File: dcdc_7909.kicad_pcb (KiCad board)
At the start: 2 copper layers, 36.8 x 26 mm, 28 parts, among them J1 V_IN, J2 G_IN, J3 +10V, J4 G_OUT, J5 -10V, U1 TMR6, U2 LT3045xMSE, U3 LT3094xMSE

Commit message: V2 PCB almost finished.
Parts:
- removed the C13 at (96.4, 76.8)
- removed the C14 at (106.4, 57.6)
- added C10: 22u, Capacitor_SMD:C_0805_2012Metric_Pad1.18x1.45mm_HandSolder, F.Cu at (91.9, 59.5)
- added C19: C_Polarized_Small, Capacitor_Tantalum_SMD:CP_EIA-3528-21_Kemet-B_Pad1.50x2.35mm_HandSolder, F.Cu at (89.0, 62.1)
- added C21: C_Polarized_Small, Capacitor_Tantalum_SMD:CP_EIA-3528-21_Kemet-B_Pad1.50x2.35mm_HandSolder, F.Cu at (94.2, 78.0)
- added C4: 2200p, Capacitor_SMD:C_0603_1608Metric, F.Cu at (107.1, 68.8)
- added C5: 22u, Capacitor_SMD:C_0805_2012Metric_Pad1.18x1.45mm_HandSolder, F.Cu at (107.5, 78.7)
- added C6: 10n, Capacitor_SMD:C_0603_1608Metric, F.Cu at (107.1, 77.0)
- added C7: 10u X7R, Capacitor_SMD:C_0603_1608Metric, F.Cu at (101.7, 65.5)
- added C8: 10u X7R, Capacitor_SMD:C_0603_1608Metric, F.Cu at (103.3, 65.5)
- added C9: 470p, Capacitor_SMD:C_0603_1608Metric, F.Cu at (105.5, 65.0)
- added D1: D_Schottky, Diode_SMD:D_PowerDI-123, F.Cu at (103.5, 72.0)
- added D2: D_Schottky, Diode_SMD:D_PowerDI-123, F.Cu at (103.5, 62.2)
- added J3: RFShield_OnePiece, RF_Shielding:Laird_Technologies_BMI-S-102_16.50x16.50mm, F.Cu at (102.0, 67.3)
- added L1: 10u, Inductor_SMD:L_Vishay_IHLP-1616, F.Cu at (97.8, 71.6)
- added L2: 10u, Inductor_SMD:L_Vishay_IHLP-1616, F.Cu at (97.8, 66.9)
- added L3: 10u, Inductor_SMD:L_Vishay_IHLP-1616, F.Cu at (97.8, 62.3)
- added R1: 20k, Resistor_SMD:R_0603_1608Metric, F.Cu at (100.5, 77.1)
- added R2: 10k, Resistor_SMD:R_0603_1608Metric, F.Cu at (107.6, 70.4)
- added R3: 1.58k, Resistor_SMD:R_0603_1608Metric, F.Cu at (108.6, 65.1)
- added R4: 10k, Resistor_SMD:R_0603_1608Metric, F.Cu at (107.1, 65.1)
- added TP1: +10.5V, TestPoint:TestPoint_Pad_D2.0mm, B.Cu at (107.1, 77.9)
- added TP2: -10.5V, TestPoint:TestPoint_Pad_D2.0mm, B.Cu at (95.6, 58.5)
- C1: value 100u 25v -> 22u; footprint Capacitor_Tantalum_SMD:CP_EIA-7343-31_Kemet-D_Pad2.25x2.55mm_HandSolder -> Capacitor_SMD:C_0805_2012Metric_Pad1.18x1.45mm_HandSolder
- C11: value 100u 16V -> 10n; footprint Capacitor_Tantalum_SMD:CP_EIA-7343-31_Kemet-D_Pad2.25x2.55mm_HandSolder -> Capacitor_SMD:C_0603_1608Metric
- C12: renamed from C4; footprint Capacitor_SMD:C_1206_3216Metric_Pad1.42x1.75mm_HandSolder -> Capacitor_SMD:C_0805_2012Metric_Pad1.18x1.45mm_HandSolder
- C13: renamed from C5; footprint Capacitor_SMD:C_1206_3216Metric_Pad1.42x1.75mm_HandSolder -> Capacitor_SMD:C_0805_2012Metric_Pad1.18x1.45mm_HandSolder
- C14: renamed from C6; footprint Capacitor_SMD:C_1206_3216Metric_Pad1.42x1.75mm_HandSolder -> Capacitor_SMD:C_0805_2012Metric_Pad1.18x1.45mm_HandSolder
- C15: renamed from C7; footprint Capacitor_SMD:C_1206_3216Metric_Pad1.42x1.75mm_HandSolder -> Capacitor_SMD:C_0805_2012Metric_Pad1.18x1.45mm_HandSolder
- C16: renamed from C8; footprint Capacitor_SMD:C_1206_3216Metric_Pad1.42x1.75mm_HandSolder -> Capacitor_SMD:C_0805_2012Metric_Pad1.18x1.45mm_HandSolder
- C17: renamed from C9; footprint Capacitor_SMD:C_0603_1608Metric_Pad1.05x0.95mm_HandSolder -> Capacitor_SMD:C_0603_1608Metric
- C18: renamed from C10; footprint Capacitor_SMD:C_1206_3216Metric_Pad1.42x1.75mm_HandSolder -> Capacitor_SMD:C_0805_2012Metric_Pad1.18x1.45mm_HandSolder
- C2: value 100u 16V -> 10u X7R; footprint Capacitor_Tantalum_SMD:CP_EIA-7343-31_Kemet-D_Pad2.25x2.55mm_HandSolder -> Capacitor_SMD:C_0603_1608Metric
- C20: renamed from C12; footprint Capacitor_SMD:C_0603_1608Metric_Pad1.05x0.95mm_HandSolder -> Capacitor_SMD:C_0603_1608Metric
- C3: value 100u 16V -> 100n X7R; footprint Capacitor_Tantalum_SMD:CP_EIA-7343-31_Kemet-D_Pad2.25x2.55mm_HandSolder -> Capacitor_SMD:C_0603_1608Metric
- D3: renamed from D1; footprint LED_SMD:LED_0603_1608Metric_Pad1.05x0.95mm_HandSolder -> LED_SMD:LED_0805_2012Metric_Pad1.15x1.40mm_HandSolder
- D4: renamed from D2; footprint LED_SMD:LED_0603_1608Metric_Pad1.05x0.95mm_HandSolder -> LED_SMD:LED_0805_2012Metric_Pad1.15x1.40mm_HandSolder
- R5: renamed from R1; value 100k -> 100k 1%; footprint Resistor_SMD:R_0603_1608Metric_Pad1.05x0.95mm_HandSolder -> Resistor_SMD:R_0603_1608Metric
- R6: renamed from R2; value 100k -> 100k 1%; footprint Resistor_SMD:R_0603_1608Metric_Pad1.05x0.95mm_HandSolder -> Resistor_SMD:R_0603_1608Metric
- R7: renamed from R3; value 820 -> 1k; footprint Resistor_SMD:R_0805_2012Metric_Pad1.15x1.40mm_HandSolder -> Resistor_SMD:R_0603_1608Metric; moved to F.Cu
- R8: renamed from R4; value 820 -> 1k; footprint Resistor_SMD:R_0805_2012Metric_Pad1.15x1.40mm_HandSolder -> Resistor_SMD:R_0603_1608Metric; moved to F.Cu
- U1: value TMR6 -> LT3471; footprint marcin_library:Traco_TMR6 -> Package_DFN_QFN:DFN-10-1EP_3x3mm_P0.5mm_EP1.65x2.38mm
- moved C3 26.1 mm to (106.8, 67.3), turned to 0 degrees
- moved C2 24.2 mm to (102.2, 78.6), turned to 0 degrees
- moved C12 23.9 mm to (81.7, 78.5), turned to 180 degrees
- moved C20 21.8 mm to (80.8, 56.0), turned to 180 degrees
- moved C14 21.8 mm to (87.0, 55.4), turned to 0 degrees
- moved C16 21.5 mm to (80.3, 68.3), turned to 90 degrees
- moved R5 19.4 mm to (87.0, 57.1), turned to 0 degrees
- moved U2 14.6 mm to (83.8, 74.4), turned to 90 degrees
- moved C18 14.4 mm to (81.3, 58.7), turned to -90 degrees
- moved C11 13.3 mm to (92.3, 65.3), turned to -90 degrees
- moved C17 10.4 mm to (82.0, 68.0)
- moved C15 10.2 mm to (85.7, 68.7), turned to 0 degrees
- moved D3 10.1 mm to (93.3, 70.9)
- moved U1 9.97 mm to (103.1, 68.8)
- moved U3 9.50 mm to (85.0, 61.1), turned to 90 degrees
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- renumbered J3 to J4, J4 to J5, J5 to J6
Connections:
- net -12V renamed /-10V
- C11 pad 1: +12V -> /-10.5V
- C12 pad 1: Net-(C2-Pad1) -> /+10.5V
- C13 pad 1: Net-(C3-Pad2) -> /-10.5V
- C16 pad 1: +12V -> /+10V
- C17 pad 1: +12V -> /+10V
- C3 pad 1: GND -> Net-(C3-Pad1)
- C3 pad 2: Net-(C3-Pad2) -> GND
- J4 pad 1: +12V -> /+10V
- R7 pad 1: +12V -> /+10V
- U1 pad 1: GND -> Net-(C4-Pad2)
- U1 pad 2: VCC -> Net-(C3-Pad1)
- U1 pad 3: VCC -> Net-(C3-Pad1)
- U1 pad 5: Net-(U1-Pad5) -> GND
- U1 pad 6: Net-(C2-Pad1) -> Net-(C7-Pad1)
- U1 pad 7: GND -> Net-(C2-Pad1)
- U1 pad 8: Net-(C3-Pad2) -> VCC
- U2 pad 1: Net-(C2-Pad1) -> /+10.5V
- U2 pad 10: +12V -> /+10V
- U2 pad 11: +12V -> /+10V
- U2 pad 12: +12V -> /+10V
- U2 pad 2: Net-(C2-Pad1) -> /+10.5V
- U2 pad 3: Net-(C2-Pad1) -> /+10.5V
- U2 pad 4: Net-(C2-Pad1) -> /+10.5V
- U2 pad 5: Net-(U2-Pad5) -> unconnected-(U2-Pad5)
- U2 pad 7: Net-(C2-Pad1) -> /+10.5V
- U3 pad 1: Net-(C3-Pad2) -> /-10.5V
- U3 pad 13: Net-(C3-Pad2) -> /-10.5V
- U3 pad 2: Net-(C3-Pad2) -> /-10.5V
- U3 pad 3: Net-(C3-Pad2) -> /-10.5V
- U3 pad 4: Net-(U3-Pad4) -> unconnected-(U3-Pad4)
- U3 pad 5: Net-(C3-Pad2) -> /-10.5V
- U3 pad 7: Net-(U3-Pad7) -> unconnected-(U3-Pad7)
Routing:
- net /+10.5V: track 0.00 -> 47.4 mm, vias 0 -> 3
- net /-10.5V: track 0.00 -> 34.0 mm, vias 0 -> 10
- net VCC: track 16.9 -> 44.4 mm, vias 0 -> 3
- net /-10V: track 13.6 -> 33.9 mm, vias 0 -> 1
- net +12V: track 14.3 -> 0.00 mm, vias 1 -> 0
- net /+10V: track 0.00 -> 12.8 mm, vias 0 -> 1
- net Net-(C3-Pad2): track 12.1 -> 0.00 mm, vias 8 -> 0
- net Net-(C2-Pad1): track 26.3 -> 15.3 mm
- net Net-(C4-Pad2): track 0.00 -> 9.00 mm
- net Net-(C9-Pad2): track 0.00 -> 7.00 mm
- net Net-(D1-Pad2): track 0.00 -> 5.19 mm
- net Net-(C7-Pad2): track 0.00 -> 4.71 mm
- net Net-(C7-Pad1): track 0.00 -> 3.82 mm
- net Net-(C3-Pad1): track 0.00 -> 2.90 mm
- net Net-(C14-Pad1): track 5.02 -> 3.57 mm
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- added copper zone on F.Cu, net /+10.5V
- added copper zone on F.Cu, net /+10V
- added copper zone on B.Cu, net /-10.5V
- added copper zone on F.Cu, net /-10.5V
- removed copper zone on F.Cu, net +12V
- removed copper zone on F.Cu, net Net-(C2-Pad1)
- removed copper zone on B.Cu, net Net-(C3-Pad2)
- removed copper zone on F.Cu, net Net-(C3-Pad2)
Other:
- board size 36.8 x 26 mm -> 37 x 27 mm
- net class Default removed
- board text added: "+"
- board text added: "+10V"
- board text added: "-10V"
- board text added: "Alpine 7909 DC/DC v2.0 (c) M. Dymczyk 07.2023"
- board text removed: "Alpine 7909 DC/DC v1.1 (c) M. Dymczyk 04.2020"
- board text removed: "Traco TMR6-1222"

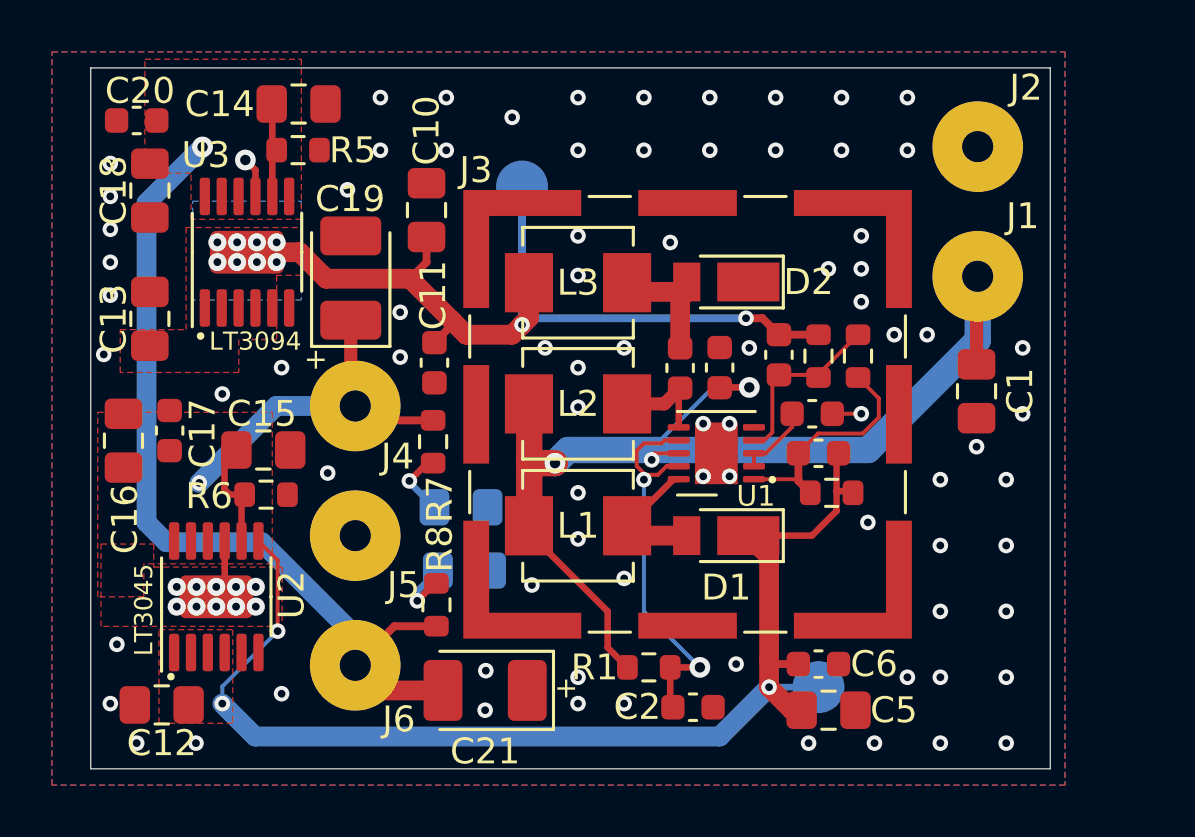
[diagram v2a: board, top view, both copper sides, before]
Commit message: One more iteration over the PCB to fit the filtering in the can.
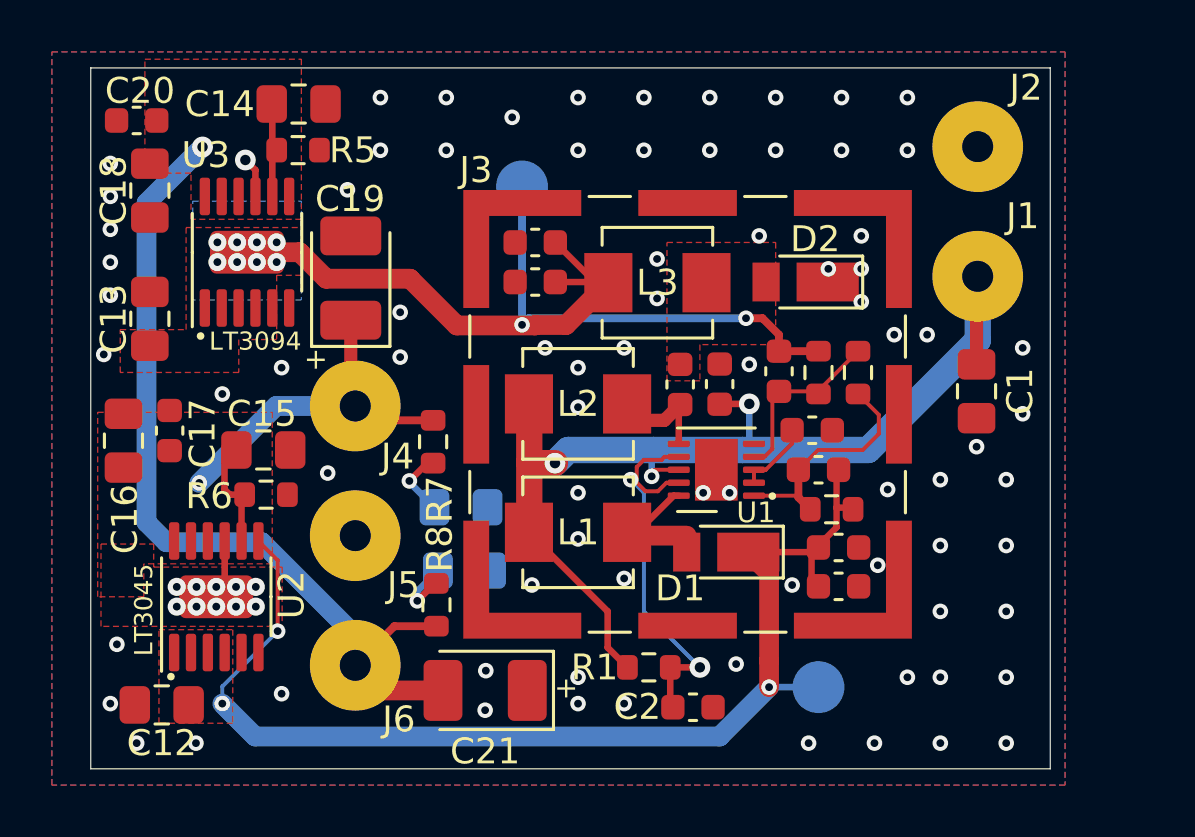
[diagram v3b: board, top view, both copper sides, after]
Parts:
- C10, C5: value 22u -> 10u; footprint Capacitor_SMD:C_0805_2012Metric_Pad1.18x1.45mm_HandSolder -> Capacitor_SMD:C_0603_1608Metric
- C12, C13, C14, C15, C16, C18, C2, C7, C8: value 10u X7R -> 10u
- C3: value 100n X7R -> 100n
- moved C11 4.98 mm to (96.1, 62.2), turned to 180 degrees
- moved C5 4.79 mm to (107.8, 74.0)
- moved C6 4.56 mm to (107.8, 72.5)
- moved C10 4.37 mm to (96.1, 60.7), turned to 180 degrees
- moved D2 3.06 mm to (106.6, 62.2)
- moved L3 3.06 mm to (100.9, 62.3)
- moved C7 0.64 mm to (101.7, 66.2)
- moved C8 0.64 mm to (103.3, 66.2)
- moved D1 0.64 mm to (103.5, 72.6)
- moved C3 0.63 mm to (106.8, 67.9)
- moved C4 0.63 mm to (107.1, 69.5)
- moved C9 0.63 mm to (105.5, 65.7)
- moved R2 0.63 mm to (107.6, 71.0)
- moved R3 0.63 mm to (108.6, 65.7)
- moved R4 0.63 mm to (107.1, 65.7)
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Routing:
- net /-10.5V: track 34.0 -> 38.3 mm
- net Net-(C7-Pad2): track 4.71 -> 0.50 mm
- net VCC: track 44.4 -> 41.8 mm
- net /+10.5V: track 47.4 -> 46.1 mm
- net GND: track 4.97 -> 3.85 mm, vias 91 -> 90
- added copper zone on F.Cu, net Net-(C7-Pad2)

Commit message: Updated ground fill zones.
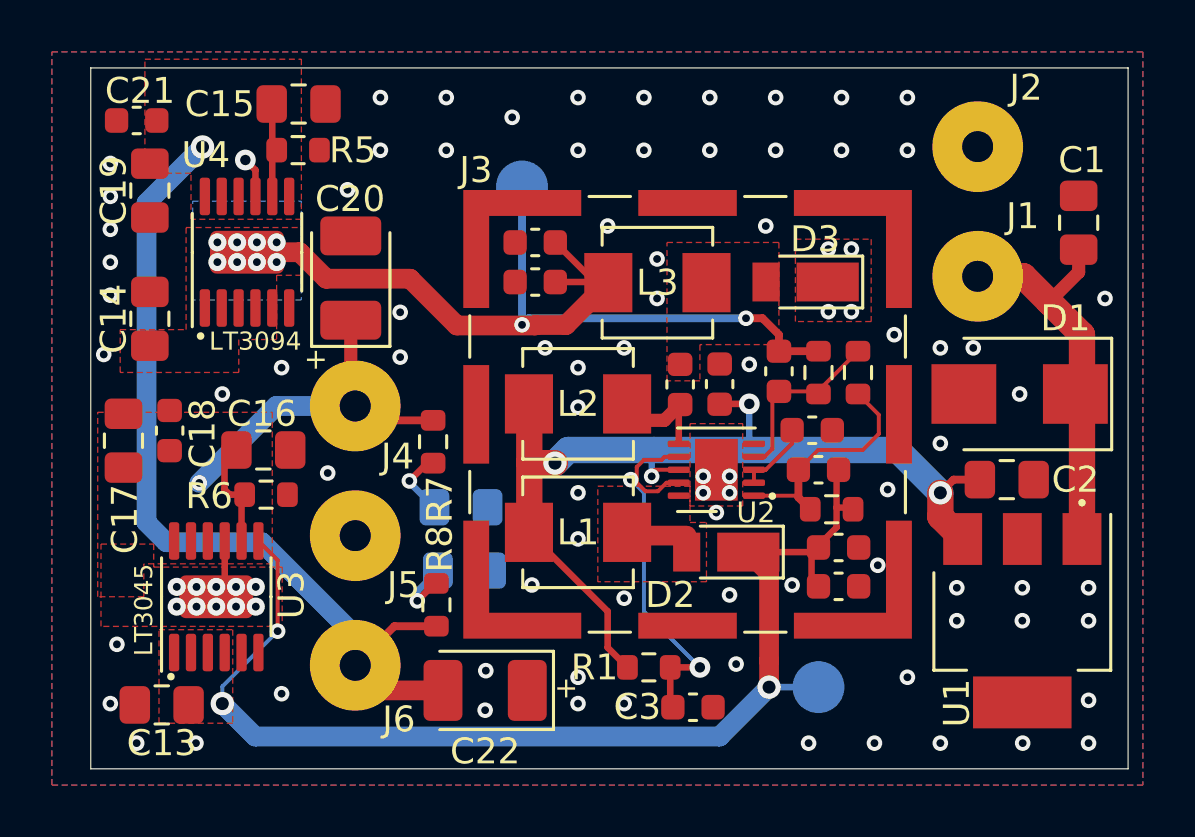
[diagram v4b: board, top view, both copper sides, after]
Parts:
- added C1: 22u, Capacitor_SMD:C_0805_2012Metric_Pad1.18x1.45mm_HandSolder, F.Cu at (117.1, 59.9)
- added D1: SM6T15A, Diode_SMD:D_SMB, F.Cu at (114.8, 66.5)
- added U1: LM2940-SOT223, Package_TO_SOT_SMD:SOT-223, F.Cu at (114.9, 75.3)
- moved C2 3.60 mm to (114.3, 69.8), turned to 0 degrees
- renumbered C9 to C10, C10 to C11, C11 to C12, C12 to C13, C13 to C14, C14 to C15, C15 to C16, C16 to C17, C17 to C18, C18 to C19, C1 to C2, C19 to C20, C20 to C21, C21 to C22, C2 to C3, C3 to C4, C4 to C5, C5 to C6, C6 to C7, C7 to C8, C8 to C9, D1 to D2, D2 to D3, D3 to D4, D4 to D5, U1 to U2, U2 to U3, U3 to U4
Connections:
- J1 pad 1: VCC -> Net-(C1-Pad1)
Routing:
- net Net-(C1-Pad1): track 0.00 -> 15.3 mm
- net VCC: track 41.8 -> 37.4 mm, vias 3 -> 4
- net Net-(D2-Pad2): track 5.19 -> 2.46 mm
- net GND: vias 90 -> 96
- added copper zone on F.Cu, net Net-(D2-Pad2)
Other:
- board size 37 x 27 mm -> 40 x 27 mm

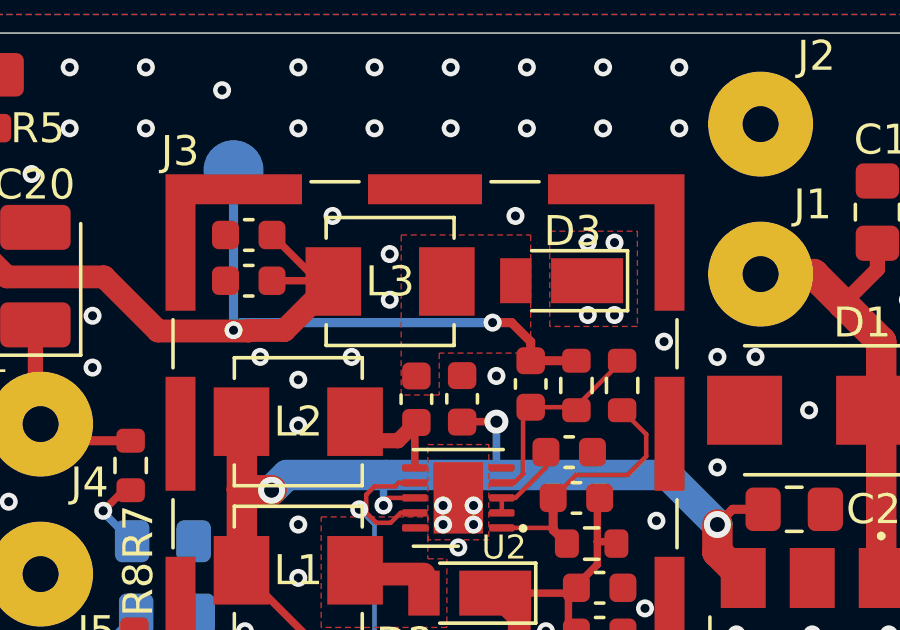
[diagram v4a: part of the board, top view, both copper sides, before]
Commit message: Updated BOM.
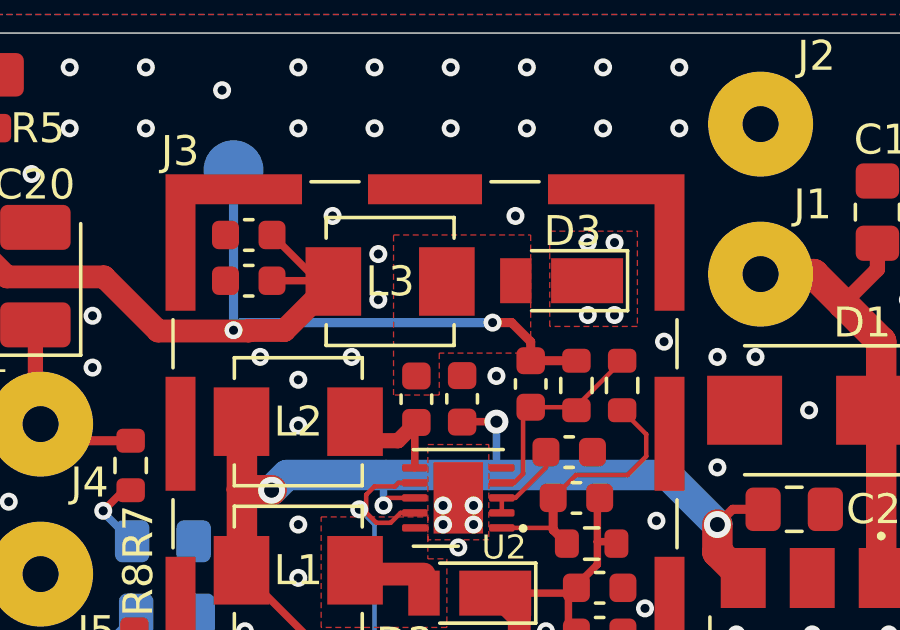
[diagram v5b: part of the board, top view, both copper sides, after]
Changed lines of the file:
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@@
   (via (at 117.475 78.359) (size 0.6) (drill 0.3) (layers "F.Cu" "B.Cu") (free) (net 2))
   (via (at 79.756 57.658) (size 0.6) (drill 0.3) (layers "F.Cu" "B.Cu") (free) (net 2))
-  (via (at 100.838 61.341) (size 0.6) (drill 0.3) (layers "F.Cu" "B.Cu") (free) (net 2))
+  (via (at 100.457 61.341) (size 0.6) (drill 0.3) (layers "F.Cu" "B.Cu") (free) (net 2))
   (via (at 114.935 80.01) (size 0.6) (drill 0.3) (layers "F.Cu" "B.Cu") (free) (net 2))
   (via (at 86.36 78.105) (size 0.6) (drill 0.3) (layers "F.Cu" "B.Cu") (free) (net 2))
@@
   (via (at 104.394 65.405) (size 0.6) (drill 0.3) (layers "F.Cu" "B.Cu") (free) (net 2))
   (via (at 79.756 58.928) (size 0.6) (drill 0.3) (layers "F.Cu" "B.Cu") (free) (net 2))
-  (via (at 100.838 62.865) (size 0.6) (drill 0.3) (layers "F.Cu" "B.Cu") (free) (net 2))
+  (via (at 100.457 62.865) (size 0.6) (drill 0.3) (layers "F.Cu" "B.Cu") (free) (net 2))
   (via (at 103.124 71.12) (size 0.6) (drill 0.3) (layers "F.Cu" "B.Cu") (free) (net 2))
   (via (at 97.79 67.056) (size 0.6) (drill 0.3) (layers "F.Cu" "B.Cu") (free) (net 2))
@@
         (xy 102.489 64.643)
         (xy 102.489 66.04)
-        (xy 101.219 66.04)
-        (xy 101.219 60.706)
+        (xy 100.965 66.04)
+        (xy 100.965 60.706)
         (xy 105.537 60.706)
       )

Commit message: Corrected the ground plane.
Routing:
- net GND: vias 96 -> 97

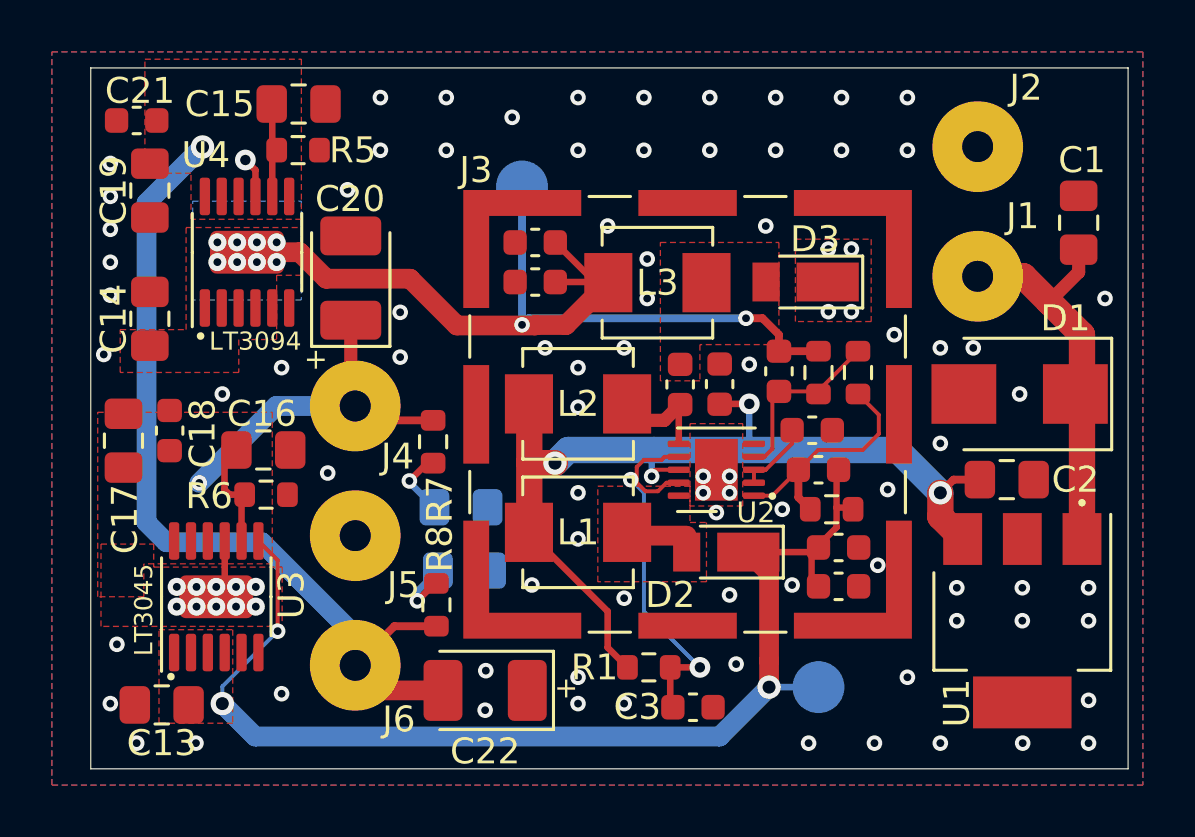
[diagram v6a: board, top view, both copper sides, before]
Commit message: New version ready for JLCPCB.
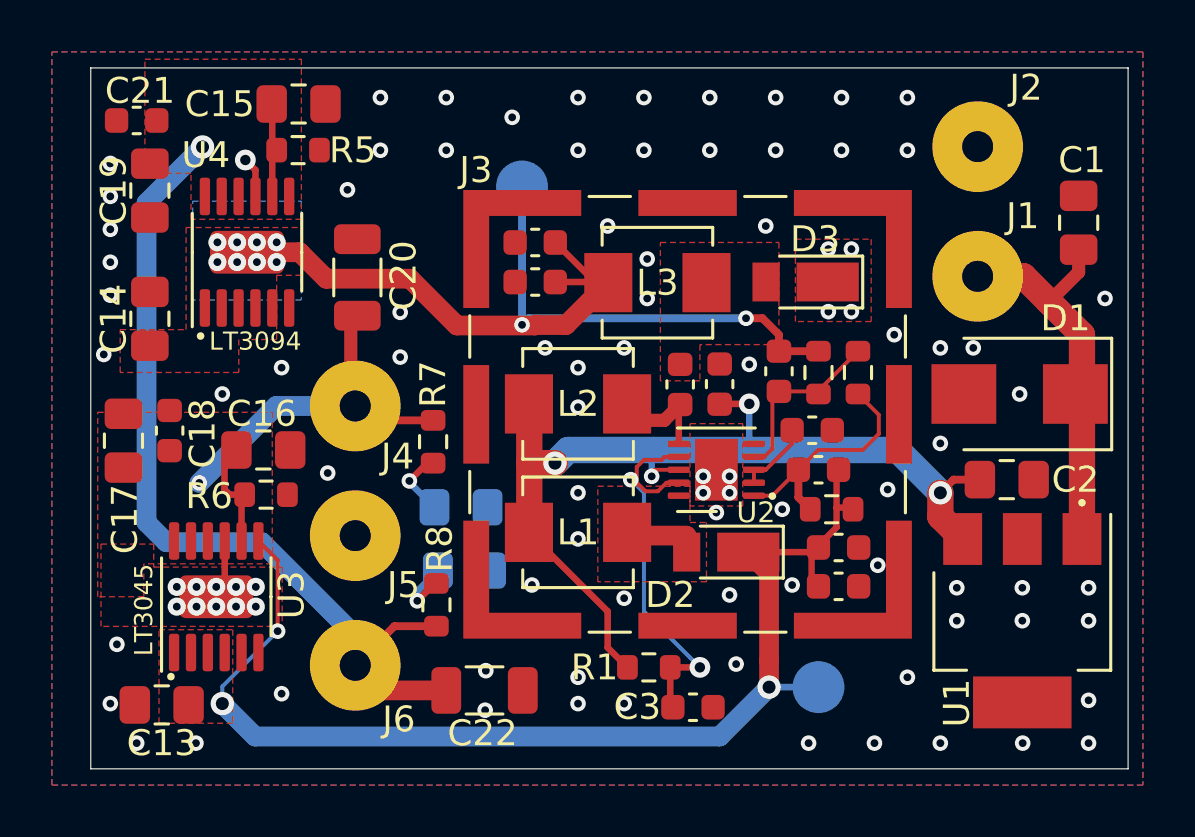
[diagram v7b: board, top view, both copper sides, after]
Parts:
- C20, C22: value C_Polarized_Small -> 22u; footprint Capacitor_Tantalum_SMD:CP_EIA-3528-21_Kemet-B_Pad1.50x2.35mm_HandSolder -> Capacitor_SMD:C_1206_3216Metric
- R2: value 10k -> 18k
- R3: value 1.58k -> 2k
- R4: value 10k -> 20k
- U1: value LM2940-SOT223 -> LM2940-SOT223-15
- moved C20 0.26 mm to (89.3, 62.1)
- turned C22 to 0 degrees
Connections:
- C22 pad 1: GND -> /-10V
- C22 pad 2: /-10V -> GND
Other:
- board text added: "Kocham R2+R3!"
- board text removed: "Kocham Rura!"
